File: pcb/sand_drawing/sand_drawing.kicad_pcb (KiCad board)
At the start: 2 copper layers, 38 parts, among them J0 12V GND, J1 Stepper1, J2 Stepper2, J3 Opto 1, J4 Opto 2, J5 UART, SW1 EN, SW2 IO0, U2 AMS1117-3.3, U3 ESP32-WROOM-32D

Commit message: More or less done. It needs to be a bit narrower, so I'm going to rejig the mounting holes.
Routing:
- net GND: vias 9 -> 11
- added copper zone on B.Cu, net GND
- added copper zone on F.Cu, net GND
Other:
- board outline added: 67 x 80.4 mm
- board text added: "EN"
- board text added: "IO0"
- board text added: "JLCJLCJLCJLC"
- board text added: "UART TX RX GND"
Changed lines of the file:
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@@
   (general
     (thickness 1.6)
-    (drawings 0)
-    (tracks 262)
+    (drawings 8)
+    (tracks 264)
     (zones 0)
     (modules 38)
@@
     (descr "Generic Phoenix Contact connector footprint for series: MCV-G; number of pins: 03; pin pitch: 3.50mm; Vertical || order number: 1843619 8A 160V")
     (tags "phoenix_contact connector MCV_01x03_G_3.5mm")
-    (fp_text reference J3 (at 6.492 -6.096) (layer F.SilkS)
+    (fp_text reference J3 (at -4.40968 -0.57404) (layer F.SilkS)
       (effects (font (size 1 1) (thickness 0.15)))
     )
@@
     (descr "Generic Phoenix Contact connector footprint for series: MCV-G; number of pins: 03; pin pitch: 3.50mm; Vertical || order number: 1843619 8A 160V")
     (tags "phoenix_contact connector MCV_01x03_G_3.5mm")
-    (fp_text reference J4 (at 3.5 -6.096) (layer F.SilkS)
+    (fp_text reference J4 (at -4.02844 -0.59436) (layer F.SilkS)
       (effects (font (size 1 1) (thickness 0.15)))
     )
@@
     (tags "capacitor 0603")
     (attr smd)
-    (fp_text reference R1 (at 2.806 0) (layer F.SilkS)
+    (fp_text reference R1 (at -2.90392 0.0762) (layer F.SilkS)
       (effects (font (size 1 1) (thickness 0.15)))
     )
@@
       (effects (font (size 1 1) (thickness 0.15)))
     )
-    (fp_line (start 1.4 0.65) (end -1.4 0.65) (layer F.CrtYd) (width 0.05))
-    (fp_line (start 1.4 0.65) (end 1.4 -0.65) (layer F.CrtYd) (width 0.05))
-    (fp_line (start -1.4 -0.65) (end -1.4 0.65) (layer F.CrtYd) (width 0.05))
-    (fp_line (start -1.4 -0.65) (end 1.4 -0.65) (layer F.CrtYd) (width 0.05))
-    (fp_line (start 0.35 0.6) (end -0.35 0.6) (layer F.SilkS) (width 0.12))
-    (fp_line (start -0.35 -0.6) (end 0.35 -0.6) (layer F.SilkS) (width 0.12))
-    (fp_line (start -0.8 -0.4) (end 0.8 -0.4) (layer F.Fab) (width 0.1))
-    (fp_line (start 0.8 -0.4) (end 0.8 0.4) (layer F.Fab) (width 0.1))
-    (fp_line (start 0.8 0.4) (end -0.8 0.4) (layer F.Fab) (width 0.1))
-    (fp_line (start -0.8 0.4) (end -0.8 -0.4) (layer F.Fab) (width 0.1))
     (fp_text user %R (at 0 0) (layer F.Fab)
       (effects (font (size 0.3 0.3) (thickness 0.075)))
     )
+    (fp_line (start -0.8 0.4) (end -0.8 -0.4) (layer F.Fab) (width 0.1))
+    (fp_line (start 0.8 0.4) (end -0.8 0.4) (layer F.Fab) (width 0.1))
+    (fp_line (start 0.8 -0.4) (end 0.8 0.4) (layer F.Fab) (width 0.1))
+    (fp_line (start -0.8 -0.4) (end 0.8 -0.4) (layer F.Fab) (width 0.1))
+    (fp_line (start -0.35 -0.6) (end 0.35 -0.6) (layer F.SilkS) (width 0.12))
+    (fp_line (start 0.35 0.6) (end -0.35 0.6) (layer F.SilkS) (width 0.12))
+    (fp_line (start -1.4 -0.65) (end 1.4 -0.65) (layer F.CrtYd) (width 0.05))
+    (fp_line (start -1.4 -0.65) (end -1.4 0.65) (layer F.CrtYd) (width 0.05))
+    (fp_line (start 1.4 0.65) (end 1.4 -0.65) (layer F.CrtYd) (width 0.05))
+    (fp_line (start 1.4 0.65) (end -1.4 0.65) (layer F.CrtYd) (width 0.05))
+    (pad 1 smd rect (at -0.75 0 180) (size 0.8 0.75) (layers F.Cu F.Paste F.Mask)
+      (net 2 +3V3))
     (pad 2 smd rect (at 0.75 0 180) (size 0.8 0.75) (layers F.Cu F.Paste F.Mask)
       (net 30 "Net-(R1-Pad2)"))
-    (pad 1 smd rect (at -0.75 0 180) (size 0.8 0.75) (layers F.Cu F.Paste F.Mask)
-      (net 2 +3V3))
     (model Capacitors_SMD.3dshapes/C_0603.wrl
       (at (xyz 0 0 0))
@@
     (descr "Through hole straight socket strip, 1x03, 2.54mm pitch, single row")
     (tags "Through hole socket strip THT 1x03 2.54mm single row")
-    (fp_text reference J5 (at 0 -2.33 90) (layer F.SilkS)
+    (fp_text reference J5 (at 2.82956 2.35204 180) (layer F.SilkS)
       (effects (font (size 1 1) (thickness 0.15)))
     )
@@
     (at 124.46 133.985 90)
     (descr "Pololu Breakout 16-pin 15.2x20.3mm 0.6x0.8\\")
-    (fp_text reference A1 (at 6.35 -2.54 90) (layer F.SilkS)
+    (fp_text reference A1 (at 6.4516 20.15744 90) (layer F.SilkS)
       (effects (font (size 1 1) (thickness 0.15)))
     )
@@
       (net 15 D1Dir))
   )
+  (gr_text "UART\nTX RX GND" (at 144.21104 97.82556) (layer F.SilkS)
+    (effects (font (size 1 1) (thickness 0.15)) (justify left))
+  )
+  (gr_text EN (at 99.43592 93.43136) (layer F.SilkS)
+    (effects (font (size 1 1) (thickness 0.15)))
+  )
+  (gr_text IO0 (at 149.16404 94.47784) (layer F.SilkS)
+    (effects (font (size 1 1) (thickness 0.15)))
+  )
+  (gr_text JLCJLCJLCJLC (at 93.726 153.86304 90) (layer F.SilkS)
+    (effects (font (size 1.5 1.5) (thickness 0.3)))
+  )
+  (gr_line (start 157.87624 164.1094) (end 157.87624 83.6676) (layer Edge.Cuts) (width 0.05))
+  (gr_line (start 90.83548 164.1094) (end 90.83548 83.6676) (layer Edge.Cuts) (width 0.05))
+  (gr_line (start 157.87624 164.1094) (end 90.83548 164.1094) (layer Edge.Cuts) (width 0.05))
+  (gr_line (start 90.83548 83.6676) (end 157.87624 83.6676) (layer Edge.Cuts) (width 0.05))
   (via (at 119.38 139.7) (size 0.8) (drill 0.4) (layers F.Cu B.Cu) (net 1))
   (segment (start 119.38 139.7) (end 119.38 137.795) (width 0.508) (layer F.Cu) (net 1))
@@
   (segment (start 140.765 96.315) (end 142.24 97.79) (width 0.508) (layer F.Cu) (net 1))
   (segment (start 132.64 96.315) (end 140.765 96.315) (width 0.508) (layer F.Cu) (net 1))
+  (via (at 128.0668 105.18648) (size 0.8) (drill 0.4) (layers F.Cu B.Cu) (net 1))
+  (via (at 139.52728 110.91164) (size 0.8) (drill 0.4) (layers F.Cu B.Cu) (net 1))
   (segment (start 111.57 129.095) (end 111.57 128.905) (width 0.25) (layer F.Cu) (net 2))
   (segment (start 106.68 133.985) (end 111.57 129.095) (width 0.25) (layer F.Cu) (net 2))
@@
   (segment (start 102.616 95.48) (end 102.64 95.504) (width 0.25) (layer F.Cu) (net 30))
   (segment (start 102.616 92.86) (end 102.616 95.48) (width 0.25) (layer F.Cu) (net 30))
+  (zone (net 0) (net_name "") (layers F&B.Cu) (hatch edge 0.508)
+    (connect_pads (clearance 0.508))
+    (min_thickness 0.254)
+    (keepout (tracks not_allowed) (vias not_allowed) (copperpour not_allowed))
+    (fill (arc_segments 32) (thermal_gap 0.508) (thermal_bridge_width 0.508))
+    (polygon
+      (pts
+        (xy 138.24712 94.75216) (xy 110.0582 94.73184) (xy 110.00232 83.67268) (xy 110.03788 83.6676) (xy 138.28776 83.6676)
+      )
+    )
+  )
+  (zone (net 1) (net_name GND) (layer F.Cu) (hatch edge 0.508)
+    (connect_pads (clearance 0.508))
+    (min_thickness 0.254)
+    (fill yes (arc_segments 32) (thermal_gap 0.508) (thermal_bridge_width 0.508))
+    (polygon
+      (pts
+        (xy 157.76956 163.99764) (xy 90.87612 164.06368) (xy 90.94216 83.7692) (xy 157.76448 83.77428)
+      )
+    )
+  )
+  (zone (net 1) (net_name GND) (layer B.Cu) (hatch edge 0.508)
+    (connect_pads (clearance 0.508))
+    (min_thickness 0.254)
+    (fill yes (arc_segments 32) (thermal_gap 0.508) (thermal_bridge_width 0.508))
+    (polygon
+      (pts
+        (xy 157.76956 163.99764) (xy 90.87612 164.06368) (xy 90.94216 83.7692) (xy 157.76448 83.77428)
+      )
+    )
+  )
 )

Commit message: Final tweaks. v1.0 PCB done!
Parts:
- removed REF** (x4): MountingHole_3.2mm_M3, Mounting_Holes:MountingHole_3.2mm_M3
- added H1: MountingHole, Mounting_Holes:MountingHole_3.2mm_M3, F.Cu at (146.3, 80.0)
- added H2: MountingHole, Mounting_Holes:MountingHole_3.2mm_M3, F.Cu at (101.5, 80.0)
- added H3: MountingHole, Mounting_Holes:MountingHole_3.2mm_M3, F.Cu at (101.5, 159.4)
- added H4: MountingHole, Mounting_Holes:MountingHole_3.2mm_M3, F.Cu at (146.3, 159.4)
- added LOGO1: OSHW-Logo2_9.8x8mm_SilkScreen, Symbols:OSHW-Logo2_9.8x8mm_SilkScreen, F.Cu at (145.8, 146.9)
- C3: value 10µF/25V -> 100pF/50V
- R1: footprint Capacitors_SMD:C_0603 -> Resistors_SMD:R_0603
- moved J3 0.75 mm to (100.2, 100.9)
- moved R1 0.19 mm to (103.4, 95.3)
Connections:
- R1 pad 2: Net-(R1-Pad2) -> Net-(C3-Pad1)
- SW1 pad 1: Net-(R1-Pad2) -> Net-(C3-Pad1)
- SW1 pad 2: Net-(C3-Pad1) -> GND
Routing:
- net GND: track 41.2 -> 55.3 mm, vias 11 -> 12
- net Net-(R1-Pad2): track 9.15 -> 0.00 mm
- net Net-(C3-Pad1): track 17.5 -> 24.3 mm
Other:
- board size 67 x 80.4 mm -> 54.2 x 89.3 mm
- board text added: "GND 12VDC"
- board text added: "GND Input1 3.3v"
- board text added: "GND Input2 3.3v"
- board text added: "Love to Michelle, Alex and Sam"
- board text added: "Sand Drawing Robot PCB v1.0 https://github.com/tjhowse/sand_drawing"
- board text added: "TX RX GND"
- board text removed: "UART TX RX GND"

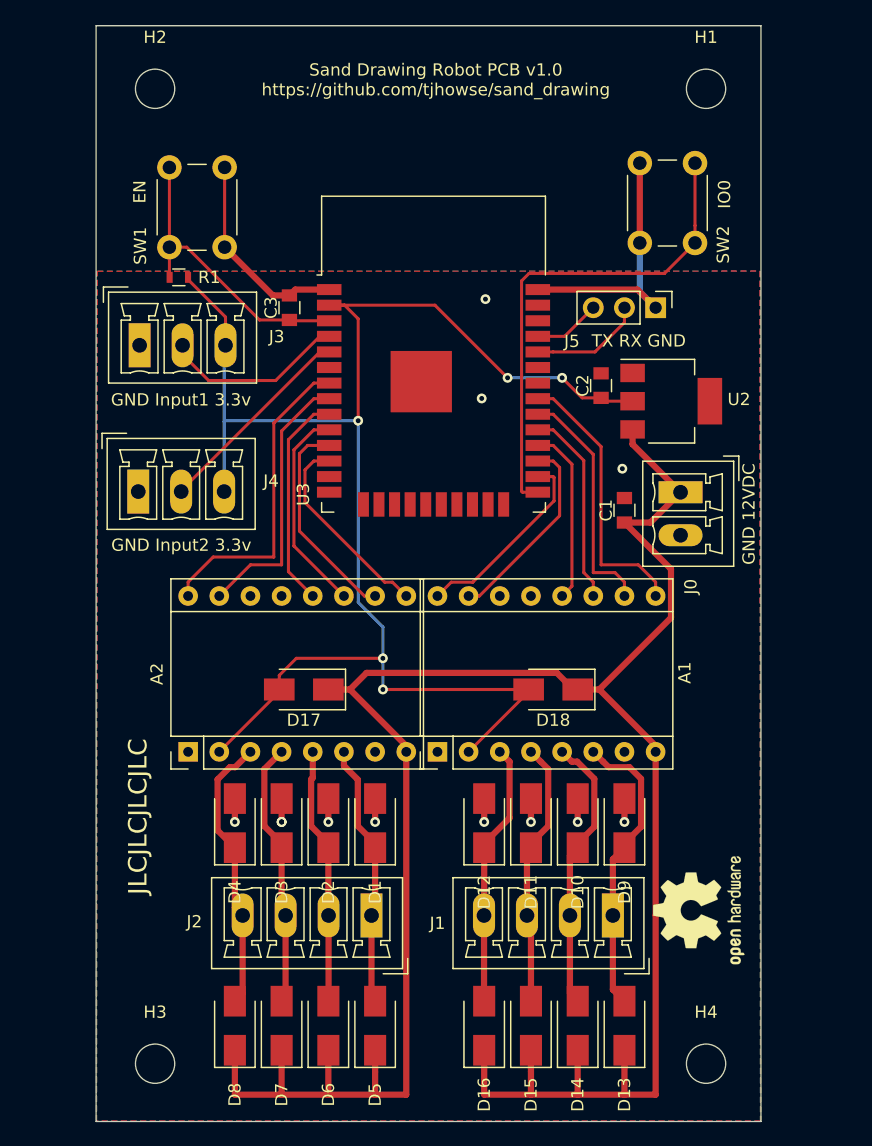
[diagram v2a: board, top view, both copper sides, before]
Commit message: PCB updates, stepper control changes.
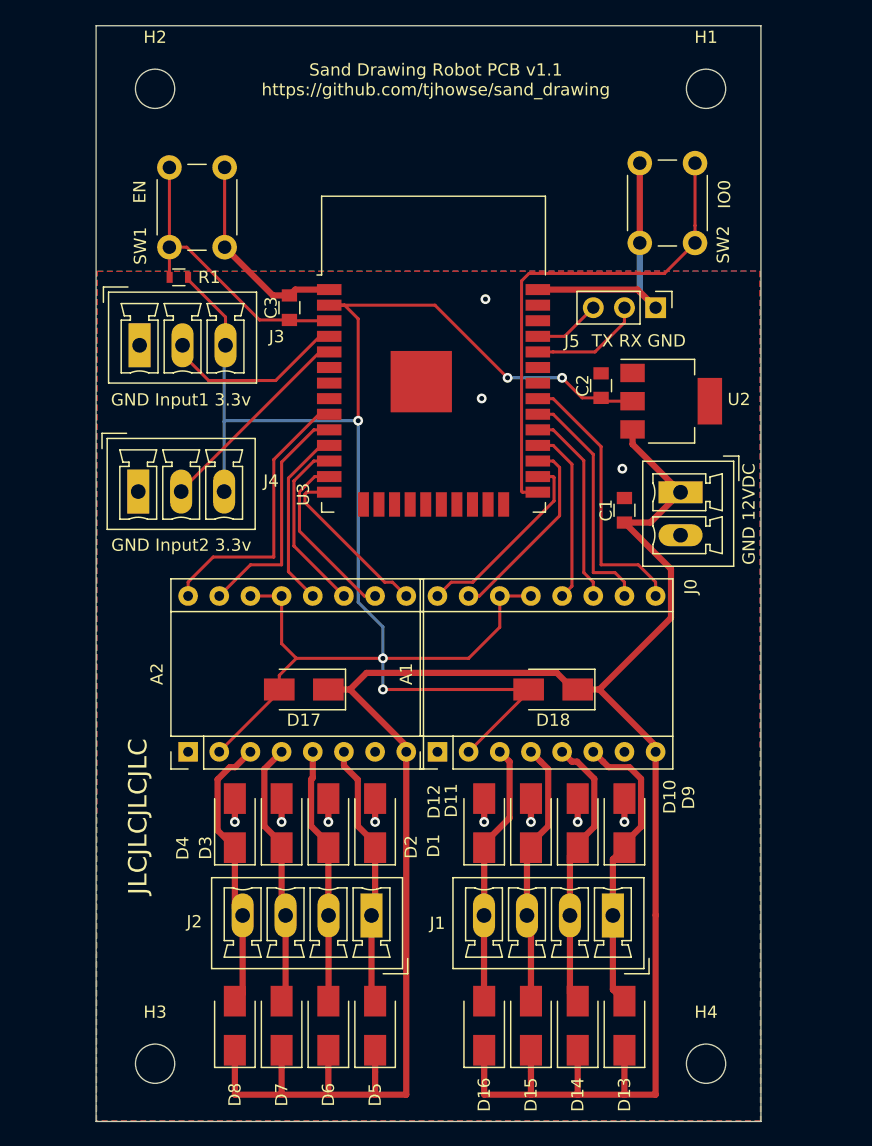
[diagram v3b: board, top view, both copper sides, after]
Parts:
- removed LOGO1: OSHW-Logo2_9.8x8mm_SilkScreen, Symbols:OSHW-Logo2_9.8x8mm_SilkScreen
- A1, A2: footprint Modules:Pololu_Breakout-16_15.2x20.3mm -> Module:Pololu_Breakout-16_15.2x20.3mm
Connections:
- A1 pad 13: (no net) -> +3V3
- A1 pad 14: (no net) -> +3V3
- A2 pad 13: (no net) -> +3V3
- A2 pad 14: (no net) -> +3V3
- U3 pad 10: D2CFG2 -> D2Step
- U3 pad 11: D2CFG1 -> D2CFG3
- U3 pad 12: D2Enable -> D2CFG2
- U3 pad 13: (no net) -> D2CFG1
- U3 pad 14: (no net) -> D2Enable
- U3 pad 16: (no net) -> unconnected-(U3-Pad16)
- U3 pad 17: (no net) -> unconnected-(U3-Pad17)
- U3 pad 18: (no net) -> unconnected-(U3-Pad18)
- U3 pad 19: (no net) -> unconnected-(U3-Pad19)
- U3 pad 20: (no net) -> unconnected-(U3-Pad20)
- U3 pad 21: (no net) -> unconnected-(U3-Pad21)
- U3 pad 22: (no net) -> unconnected-(U3-Pad22)
- U3 pad 23: (no net) -> unconnected-(U3-Pad23)
- U3 pad 24: (no net) -> unconnected-(U3-Pad24)
- U3 pad 32: (no net) -> unconnected-(U3-Pad32)
- U3 pad 33: (no net) -> unconnected-(U3-Pad33)
- U3 pad 36: (no net) -> unconnected-(U3-Pad36)
- U3 pad 37: (no net) -> unconnected-(U3-Pad37)
- U3 pad 6: (no net) -> unconnected-(U3-Pad6)
- U3 pad 7: D2Dir -> unconnected-(U3-Pad7)
- U3 pad 8: D2Step -> unconnected-(U3-Pad8)
- U3 pad 9: D2CFG3 -> D2Dir
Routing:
- net +3V3: track 128.1 -> 151.4 mm
- net D2CFG3: track 17.7 -> 14.9 mm
- net D2CFG1: track 17.4 -> 14.5 mm
- net D2Dir: track 25.7 -> 23.0 mm
- net D2Step: track 22.0 -> 19.5 mm
- net D2CFG2: track 17.2 -> 14.6 mm
- net D2Enable: track 16.3 -> 14.1 mm
- net GND: track 55.3 -> 54.6 mm, vias 12 -> 11
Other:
- net class Default removed
- net class Power removed
- board text added: "Sand Drawing Robot PCB v1.1 https://github.com/tjhowse/sand_drawing"
- board text removed: "Sand Drawing Robot PCB v1.0 https://github.com/tjhowse/sand_drawing"

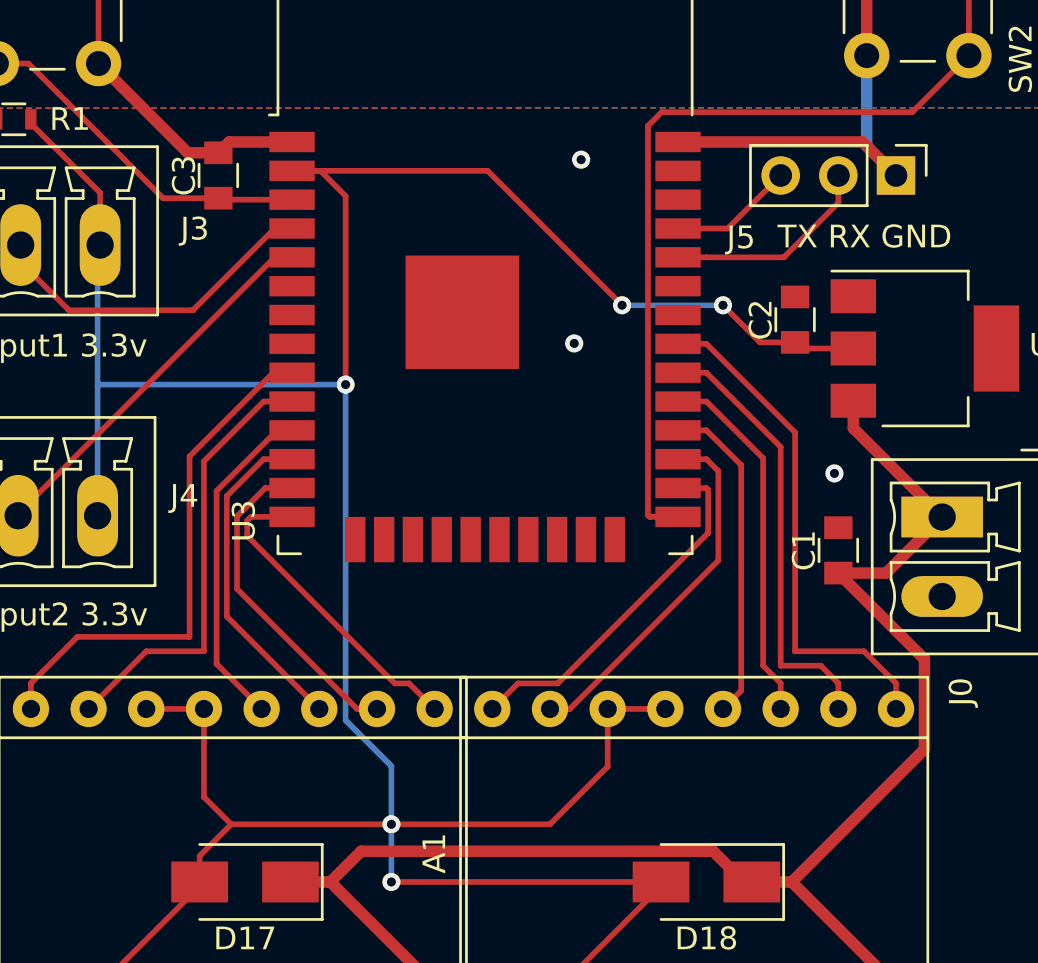
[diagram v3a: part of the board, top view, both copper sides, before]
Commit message: Update PCB and schematic to map all stepper control pins to GPIO.
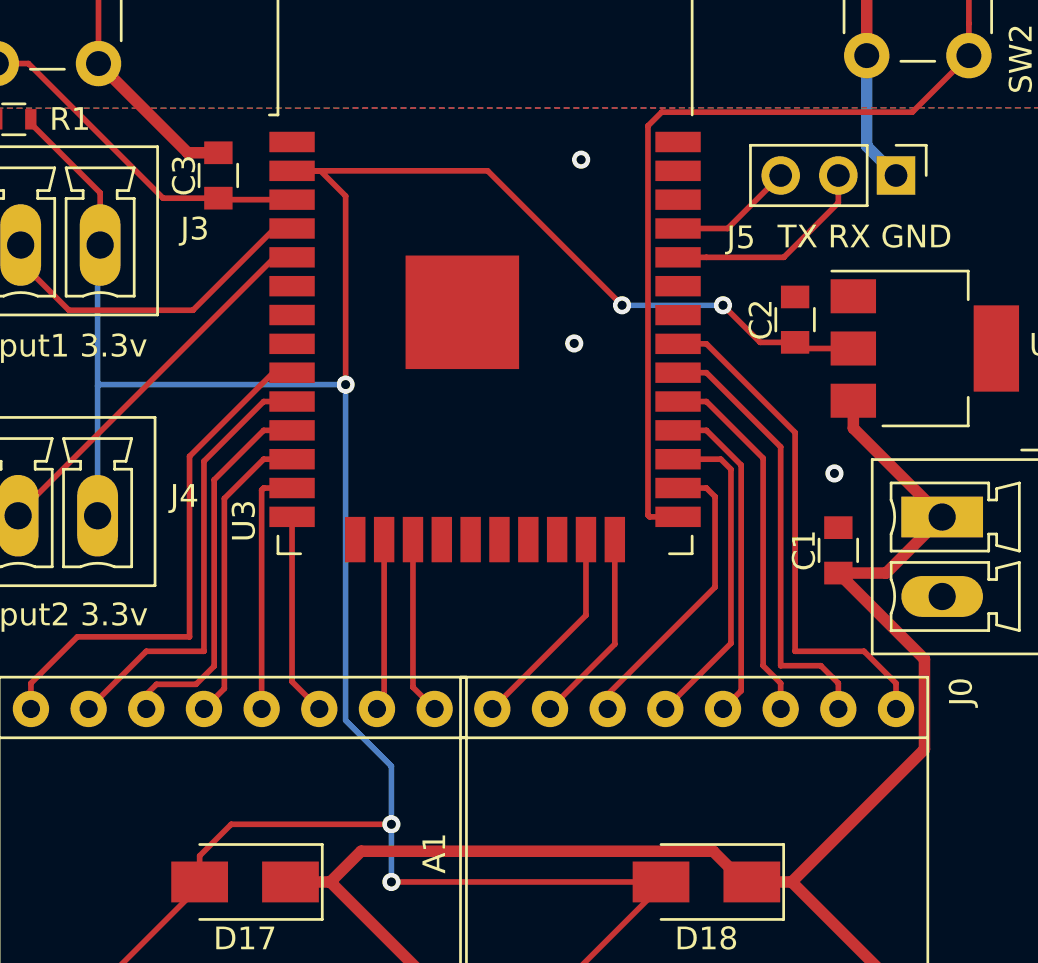
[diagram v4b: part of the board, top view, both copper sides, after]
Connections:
- A1 pad 13: +3V3 -> D1Rst
- A1 pad 14: +3V3 -> D1Slp
- A2 pad 13: +3V3 -> D2Rst
- A2 pad 14: +3V3 -> D2Slp
- U3 pad 11: D2CFG3 -> D2Slp
- U3 pad 12: D2CFG2 -> D2Rst
- U3 pad 13: D2CFG1 -> D2CFG3
- U3 pad 14: D2Enable -> D2CFG2
- U3 pad 16: unconnected-(U3-Pad16) -> D2CFG1
- U3 pad 17: unconnected-(U3-Pad17) -> D2Enable
- U3 pad 23: unconnected-(U3-Pad23) -> D1Dir
- U3 pad 24: unconnected-(U3-Pad24) -> D1Step
- U3 pad 26: D1Dir -> D1Slp
- U3 pad 27: D1Step -> D1Rst
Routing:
- net +3V3: track 151.4 -> 127.6 mm
- net D2Slp: track 0.00 -> 16.5 mm
- net D1Rst: track 0.00 -> 13.8 mm
- net GND: track 54.6 -> 41.0 mm
- net D1Slp: track 0.00 -> 12.9 mm
- net D2Rst: track 0.00 -> 12.9 mm
- net D1Step: track 16.1 -> 8.64 mm
- net D2CFG1: track 14.5 -> 7.59 mm
- net D1Dir: track 16.0 -> 9.17 mm
- net D2Enable: track 14.1 -> 7.86 mm
- net D2CFG2: track 14.6 -> 8.96 mm
- net D2CFG3: track 14.9 -> 11.0 mm

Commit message: v1.1 of the PCB nearly done.
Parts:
- removed D18: SS210 Schottky Diode, Diode_SMD:D_SMA
- removed the U2 at (143.5, 105.4)
- added C3: 100nF/50V, Capacitor_SMD:C_0603_1608Metric, F.Cu at (146.1, 107.5)
- added C5: 22µF/25V, Capacitor_SMD:C_1206_3216Metric, F.Cu at (141.4, 107.1)
- added C6: 100nF/50V, Capacitor_SMD:C_0603_1608Metric, F.Cu at (145.4, 115.9)
- added L1: 6.8µH, sand_drawing_parts:WURTH_6060, F.Cu at (141.0, 114.3)
- added U1: AP63203WU, Package_TO_SOT_SMD:TSOT-23-6, F.Cu at (146.8, 112.6)
- C2: renamed from C1; value 10µF/25V -> 10µF/35V; footprint Capacitors_SMD:C_0805 -> Capacitor_SMD:C_1206_3216Metric
- C4: renamed from C2; value 10µF/25V -> 22µF/25V; footprint Capacitors_SMD:C_0805 -> Capacitor_SMD:C_1206_3216Metric
- moved J0 13.8 mm to (144.0, 99.0)
- moved D17 12.9 mm to (123.2, 137.6), turned to 0 degrees
- moved D1 12.0 mm to (119.5, 127.8)
- moved D10 12.0 mm to (136.0, 127.8)
- moved D11 12.0 mm to (132.2, 127.8)
- moved D12 12.0 mm to (128.4, 127.8)
- moved D2 12.0 mm to (115.7, 127.8)
- moved D3 12.0 mm to (111.8, 127.8)
- moved D4 12.0 mm to (108.0, 127.8)
- moved D9 12.0 mm to (139.8, 127.8)
- moved C2 8.01 mm to (146.2, 109.6), turned to 180 degrees
- moved J5 7.83 mm to (136.3, 102.9), turned to 180 degrees
- moved H3 7.77 mm to (101.5, 151.6)
- moved H4 7.77 mm to (146.3, 151.6)
- moved C4 6.57 mm to (141.4, 109.6), turned to 0 degrees
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- renumbered C3 to C1, U3 to U2
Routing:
- net +12V: track 179.9 -> 121.5 mm
- net +3V3: track 127.6 -> 142.0 mm
- net GND: track 41.0 -> 33.7 mm
- net Net-(C6-Pad1): track 0.00 -> 6.81 mm
- net RX: track 9.26 -> 4.11 mm
- net Net-(A1-Pad6): track 24.3 -> 22.4 mm
- net Net-(C6-Pad2): track 0.00 -> 1.68 mm
- net Net-(A2-Pad3): track 22.8 -> 21.3 mm
- net Net-(A1-Pad5): track 22.7 -> 21.4 mm
- net Net-(A2-Pad4): track 21.8 -> 20.6 mm
- net Net-(A1-Pad4): track 21.8 -> 20.6 mm
- net TX: track 5.49 -> 4.64 mm
- net Net-(A2-Pad6): track 21.6 -> 22.4 mm
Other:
- board size 54.2 x 89.3 mm -> 54.2 x 81.5 mm
- board text removed: "JLCJLCJLCJLC"
